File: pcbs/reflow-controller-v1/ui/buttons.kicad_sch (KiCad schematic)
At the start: 18 parts, among them SW1001 TS04-66-85-BK-160-SMT, SW1002 PEC12R-3220F-S0024, SW1003 TS04-66-85-BK-160-SMT

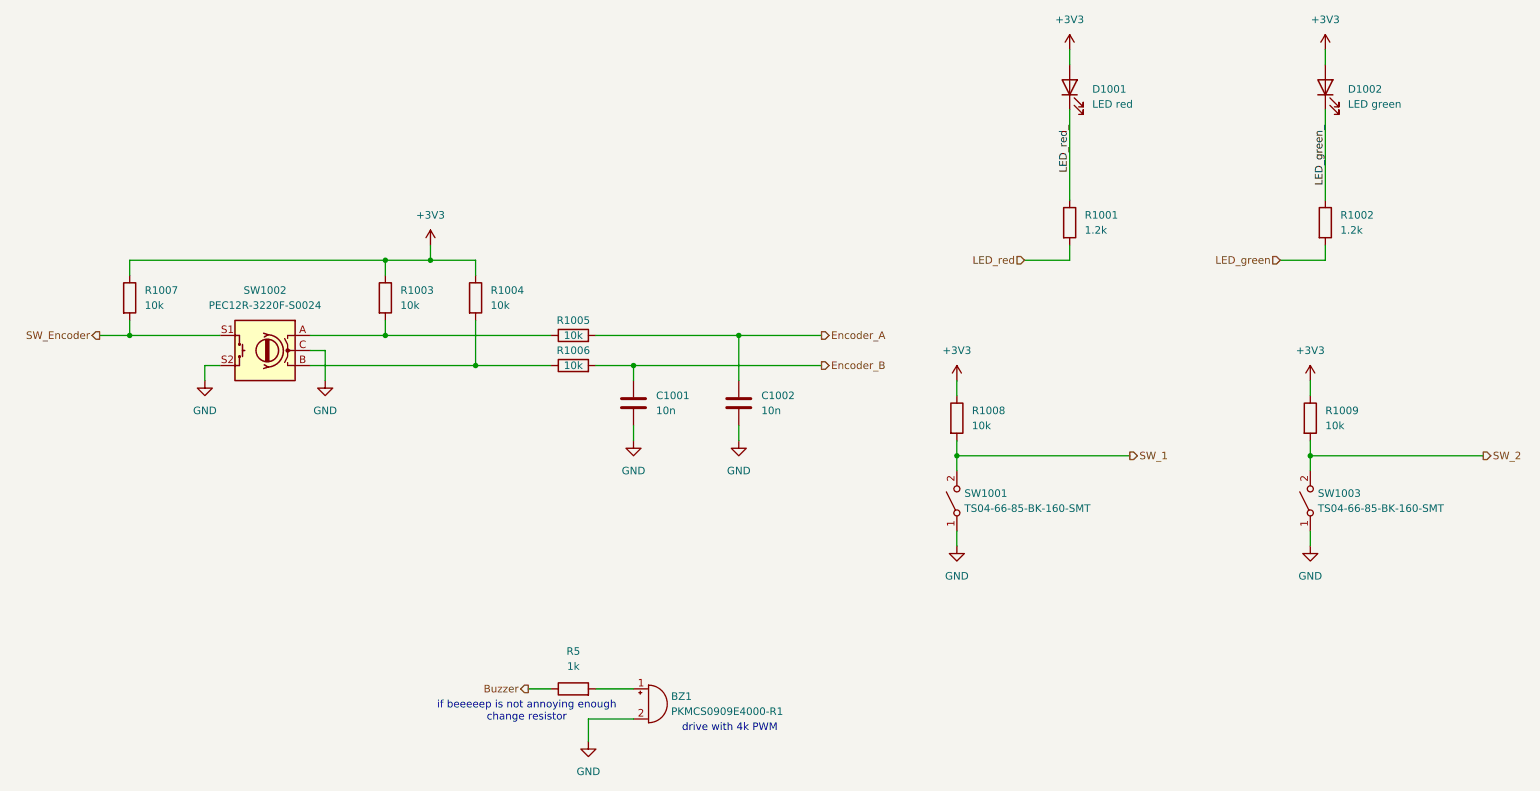
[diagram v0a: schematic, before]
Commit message: split pcbs into two for safety
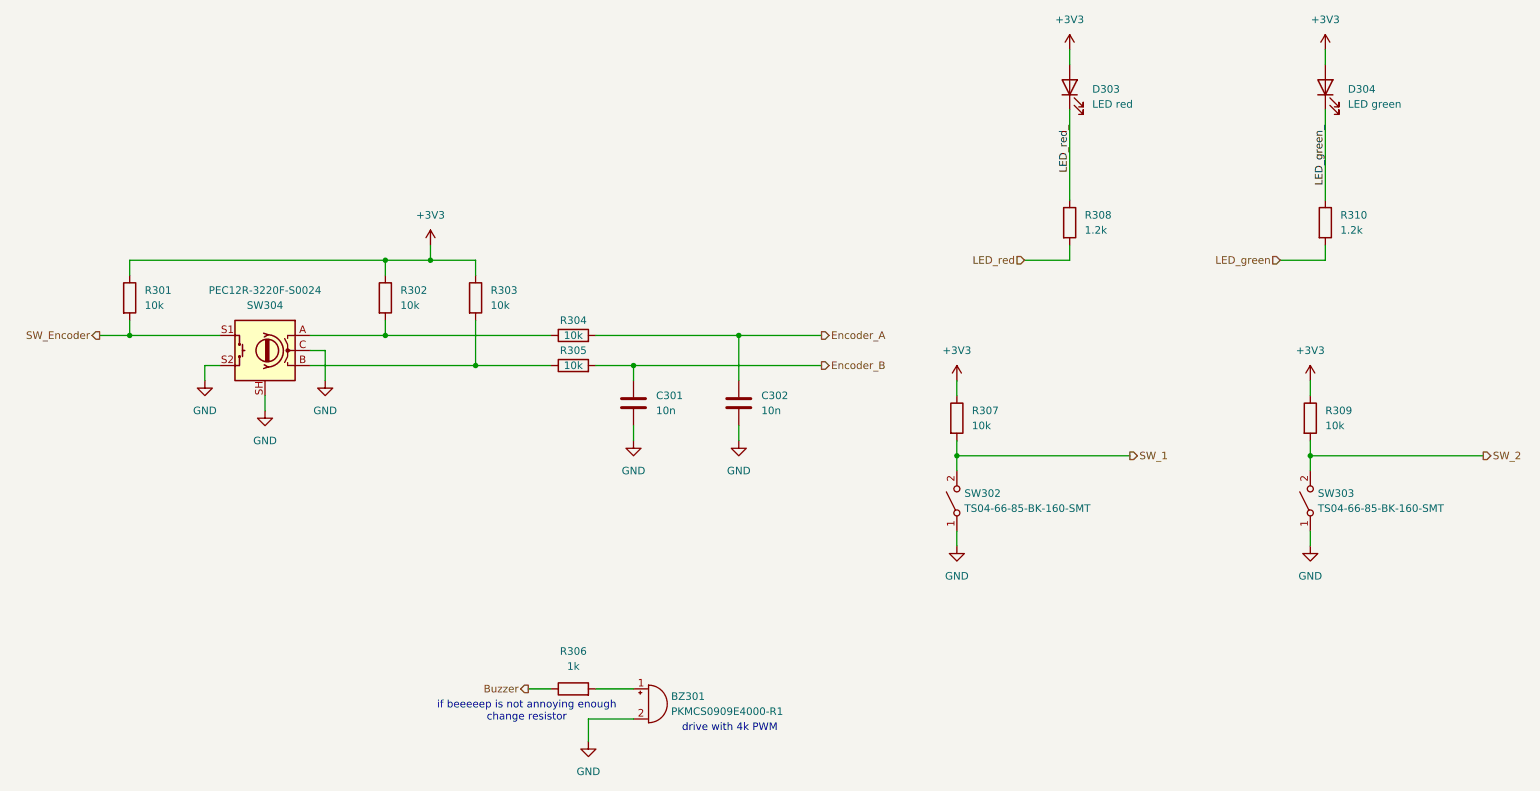
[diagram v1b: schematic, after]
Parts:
- removed D1001: LED red, LED_SMD:LED_0603_1608Metric, symbol Device:LED
- removed D1002: LED green, LED_SMD:LED_0603_1608Metric, symbol Device:LED
- removed SW1002: PEC12R-3220F-S0024, Rotary_Encoder:RotaryEncoder_Bourns_Vertical_PEC12R-3x17F-Sxxxx, symbol Device:RotaryEncoder_Switch
- added D303: LED red, Diode_SMD:D_0603_1608Metric, symbol Device:LED
- added D304: LED green, Diode_SMD:D_0603_1608Metric, symbol Device:LED
- added SW304: PEC12R-3220F-S0024, Rotary_Encoder:RotaryEncoder_Bourns_Vertical_PEC12R-3x17F-Sxxxx, symbol Device:RotaryEncoder_Switch_MP
- SW302: renamed from SW1001; footprint Button_Switch_SMD:SW_Push_1P1T_NO_6x6mm_H9.5mm -> Button_Switch_SMD:SW_SPST_PTS647_Sx70
- SW303: renamed from SW1003; footprint Button_Switch_SMD:SW_Push_1P1T_NO_6x6mm_H9.5mm -> Button_Switch_SMD:SW_SPST_PTS647_Sx70
- renumbered BZ1 to BZ301, C1001 to C301, C1002 to C302, R1007 to R301, R1003 to R302, R1004 to R303, R1005 to R304, R1006 to R305, R5 to R306, R1008 to R307, R1001 to R308, R1009 to R309, R1002 to R310
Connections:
- net +3V3: now also D303.2 (A), D304.2 (A)
- net GND: now also SW304.C, SW304.S2, SW304.SH
- net LED_green_: now also D304.1 (K)
- net LED_red_: now also D303.1 (K)
- net SW_Encoder: now also SW304.S1
- net at R302.2, R304.1: now also SW304.A
- net at R303.2, R305.1: now also SW304.B
